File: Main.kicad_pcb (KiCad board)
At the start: 2 copper layers, 99.1 x 78.7 mm, 45 parts, among them J1 Conn_01x01_Female, J10 Conn_01x01_Female, J11 Conn_01x01_Female, J12 Conn_01x01_Female, J2 Conn_01x01_Female, J3 Conn_01x01_Female, J4 Conn_01x02_Female, J5 Conn_01x01_Female, J6 Conn_01x03, J7 Conn_01x03, J8 Conn_01x06, J9 Conn_01x01_Female, Q1 CSD17307Q5A, Q2 CSD17307Q5A, Q3 Si6435ADQ, SW1 SW_Push, SW2 SW_Push, SW3 SW_Push, SW4 SW_Push, U1 LTC4002ES8-4.2, U3 LTC6995-1, U4 TPS2557

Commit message: changes for BOM
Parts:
- moved C6 48.7 mm to (64.7, 91.9)
- moved BT1 48.7 mm to (73.3, 36.3)
- moved C4 48.7 mm to (89.1, 51.0)
- moved C5 48.7 mm to (85.0, 51.0)
- moved D1 48.7 mm to (101.0, 58.4)
- moved D2 48.7 mm to (102.0, 65.4)
- moved J1 48.7 mm to (28.6, 72.8)
- moved J10 48.7 mm to (75.8, 93.3)
- moved J12 48.7 mm to (95.0, 60.2)
- moved J2 48.7 mm to (48.6, 72.8)
- moved J3 48.7 mm to (49.6, 75.8)
- moved J4 48.7 mm to (49.6, 95.8)
- moved J5 48.7 mm to (29.6, 97.8)
- moved J6 48.7 mm to (41.7, 52.1)
- moved J7 48.7 mm to (57.0, 52.1)
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
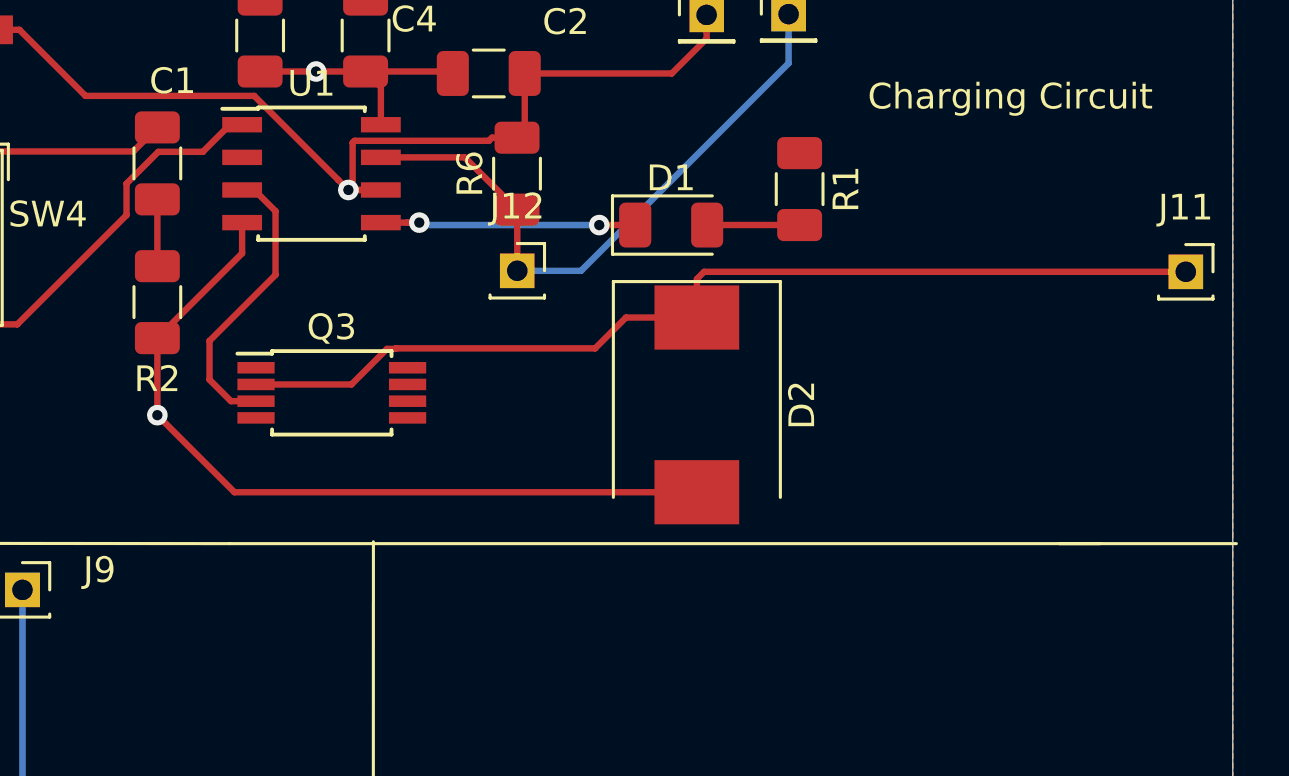
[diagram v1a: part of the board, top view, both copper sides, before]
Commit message: changed transistor
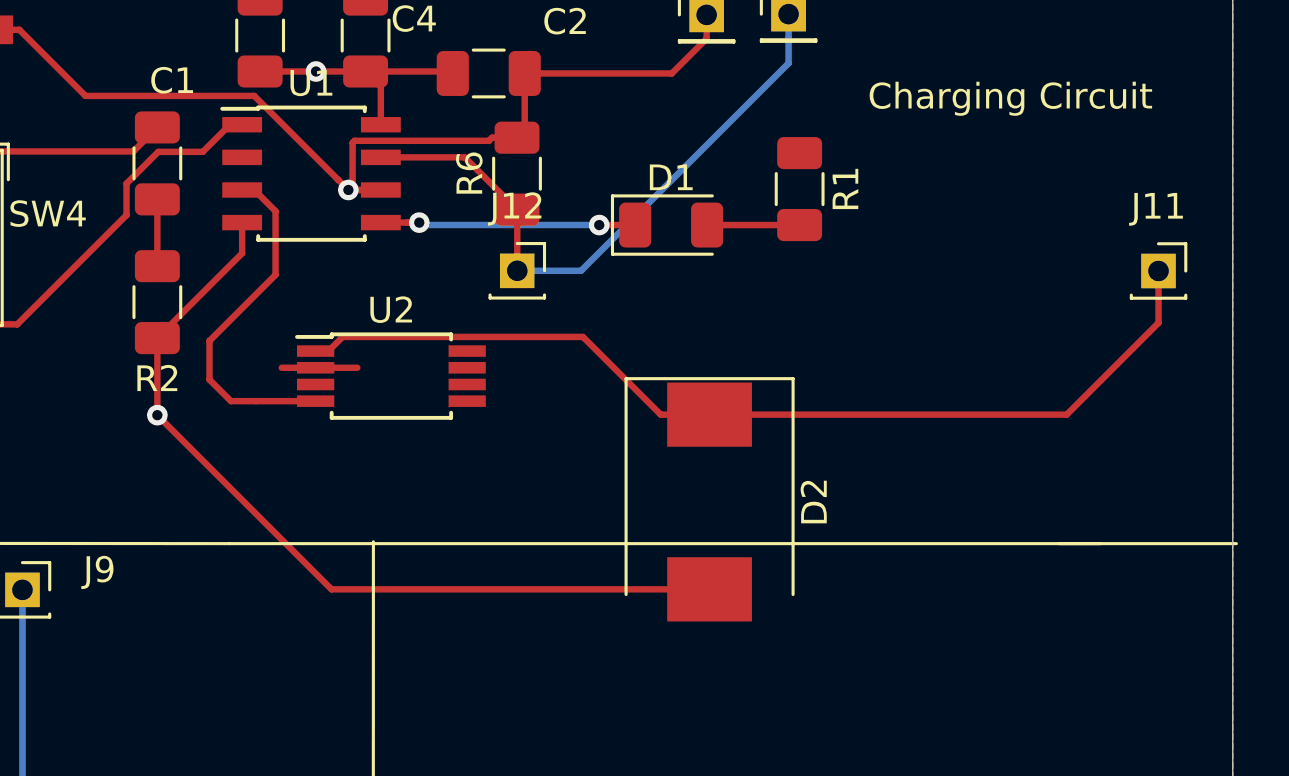
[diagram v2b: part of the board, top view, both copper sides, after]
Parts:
- removed Q3: Si6435ADQ, Package_SO:TSSOP-8_4.4x3mm_P0.65mm
- added U2: SI6423, Package_SO:TSSOP-8_4.4x3mm_P0.65mm, F.Cu at (90.1, 64.3)
- moved D2 3.81 mm to (102.5, 69.2)
- moved J11 1.06 mm to (120.0, 60.2)
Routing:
- net +5V: track 0.00 -> 3.42 mm
- net Net-(U1-Pad3): track 11.4 -> 13.7 mm
- net GNDD: track 78.7 -> 80.8 mm
- net Net-(D2-Pad1): track 38.9 -> 37.8 mm
